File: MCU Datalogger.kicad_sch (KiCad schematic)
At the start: 0 parts

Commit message: Have added required symbols to schematic sheets.
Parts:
- added BT1: Battery, symbol Device:Battery
- added C1, C2, C3, C4, C5: C, symbol Device:C
- added C6: C_Polarized_US, symbol Device:C_Polarized_US
- added D1, D2: LED, symbol Device:LED
- added H1, H2, H3, H4: MountingHole, symbol Mechanical:MountingHole
- added R1, R2, R3, R4, R5, R6, R7: R_US, symbol Device:R_US
- added U1, U2: 24LC1025, symbol Memory_EEPROM:24LC1025
- added U3: DS1337S_, DS1337S_:SOIC127P600X175-8N, symbol DS1337S_:DS1337S_
- added U4: ATMEGA328P-AU, ATMEGA328P-AU:QFP80P900X900X120-32N, symbol ATMEGA328P-AU:ATMEGA328P-AU
- added Y1, Y2: Crystal, symbol Device:Crystal
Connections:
- new net: U4.21 (GND), U4.3 (GND), U4.5 (GND)
- new net: U4.4 (VCC), U4.6 (VCC)
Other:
- added sheet Connectors (connectors.kicad_sch)

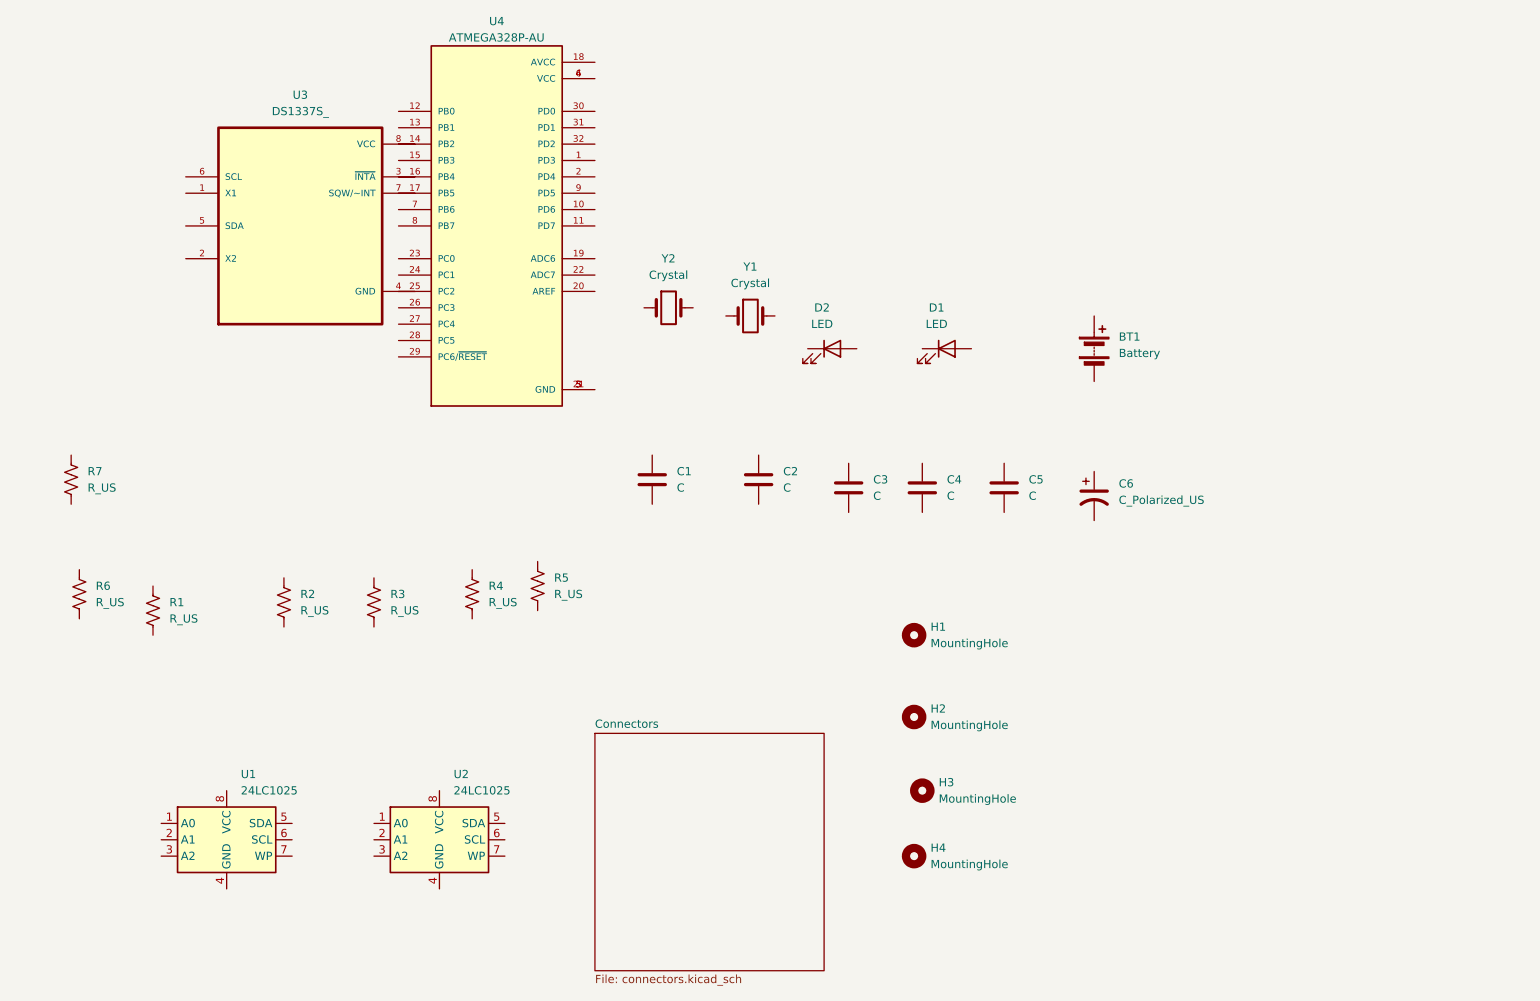
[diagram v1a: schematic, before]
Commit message: Changed locations of symbols (arrange).
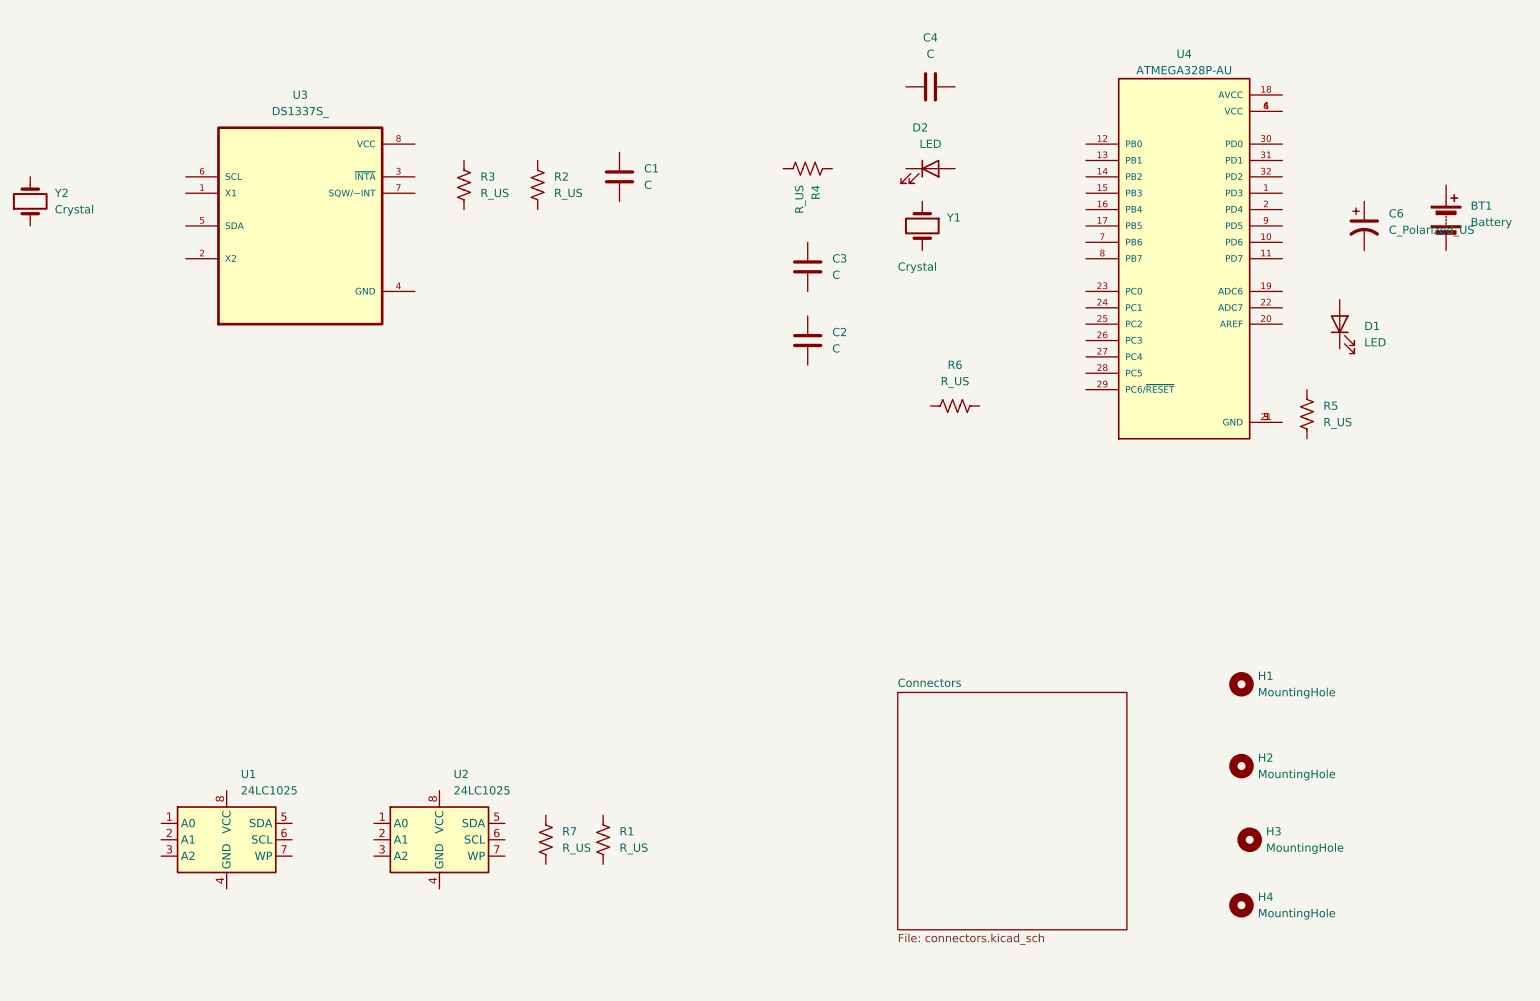
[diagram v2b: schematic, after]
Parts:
- removed C5: C, symbol Device:C
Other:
- moved on the sheet: BT1, C1, C2, C3, C4, C6, D1, D2, H1, H2, H3, H4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

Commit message: Added component values.
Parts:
- C1, C4: value C -> 0.1uF
- C2, C3: value C -> 22pF
- C6: value C_Polarized_US -> 100nF
- R1, R7: value R_US -> 4.7k
- R2, R3, R6: value R_US -> 10k
- R4, R5: value R_US -> 330
- Y1: value Crystal -> 16 MHz
- Y2: value Crystal -> 32.768 KHz
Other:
- moved on the sheet: C6
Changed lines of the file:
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@@
 			)
 		)
-		(property "Value" "C"
+		(property "Value" "22pF"
 			(at 166.37 63.4999 0)
 			(effects
@@
 			)
 		)
-		(property "Value" "Crystal"
+		(property "Value" "16 MHz"
 			(at 176.53 50.8 90)
 			(effects
@@
 			)
 		)
-		(property "Value" "R_US"
+		(property "Value" "4.7k"
 			(at 124.46 140.9699 0)
 			(effects
@@
 		(dnp no)
 		(property "Reference" "R4"
-			(at 163.8301 38.1 0)
-			(effects
-				(font
-					(size 1.27 1.27)
-				)
-				(justify left)
-			)
-		)
-		(property "Value" "R_US"
-			(at 161.2901 38.1 0)
+			(at 161.29 39.37 90)
+			(effects
+				(font
+					(size 1.27 1.27)
+				)
+				(justify left)
+			)
+		)
+		(property "Value" "330"
+			(at 160.02 31.75 90)
 			(effects
 				(font
@@
 			)
 		)
-		(property "Value" "R_US"
+		(property "Value" "4.7k"
 			(at 133.35 140.97 0)
 			(effects
@@
 			)
 		)
-		(property "Value" "C"
+		(property "Value" "0.1uF"
 			(at 181.61 17.78 90)
 			(effects
@@
 				)
 				(hide yes)
+			)
+		)
+		(property "Purpose" ""
+			(at 181.61 22.86 0)
+			(effects
+				(font
+					(size 1.27 1.27)
+				)
 			)
 		)
@@
 			)
 		)
-		(property "Value" "C"
+		(property "Value" "0.1uF"
 			(at 137.16 38.0999 0)
 			(effects
@@
 			)
 		)
-		(property "Value" "R_US"
+		(property "Value" "330"
 			(at 242.57 74.9299 0)
 			(effects
@@
 	(symbol
 		(lib_id "Device:C_Polarized_US")
-		(at 248.92 44.45 0)
+		(at 247.65 41.91 0)
 		(unit 1)
 		(exclude_from_sim no)
@@
 		(fields_autoplaced yes)
 		(property "Reference" "C6"
-			(at 252.73 42.5449 0)
-			(effects
-				(font
-					(size 1.27 1.27)
-				)
-				(justify left)
-			)
-		)
-		(property "Value" "C_Polarized_US"
-			(at 252.73 45.0849 0)
-			(effects
-				(font
-					(size 1.27 1.27)
-				)
-				(justify left)
-			)
-		)
-		(property "Footprint" ""
-			(at 248.92 44.45 0)
+			(at 251.46 40.0049 0)
+			(effects
+				(font
+					(size 1.27 1.27)
+				)
+				(justify left)
+			)
+		)
+		(property "Value" "100nF"
+			(at 251.46 42.5449 0)
+			(effects
+				(font
+					(size 1.27 1.27)
+				)
+				(justify left)
+			)
+		)
+		(property "Footprint" ""
+			(at 247.65 41.91 0)
 			(effects
 				(font
@@
 		)
 		(property "Datasheet" "~"
-			(at 248.92 44.45 0)
+			(at 247.65 41.91 0)
 			(effects
 				(font
@@
 		)
 		(property "Description" "Polarized capacitor, US symbol"
-			(at 248.92 44.45 0)
+			(at 247.65 41.91 0)
 			(effects
 				(font
@@
 			)
 		)
-		(property "Value" "R_US"
+		(property "Value" "10k"
 			(at 185.42 68.58 90)
 			(effects
@@
 			)
 		)
-		(property "Value" "R_US"
+		(property "Value" "10k"
 			(at 111.76 39.3699 0)
 			(effects
@@
 				)
 				(hide yes)
+			)
+		)
+		(property "Purpose" ""
+			(at 109.22 38.1 0)
+			(effects
+				(font
+					(size 1.27 1.27)
+				)
 			)
 		)
@@
 			)
 		)
-		(property "Value" "R_US"
+		(property "Value" "10k"
 			(at 123.19 39.3699 0)
 			(effects
@@
 			)
 		)
-		(property "Value" "Crystal"
+		(property "Value" "32.768 KHz"
 			(at 45.72 41.9099 90)
 			(effects
@@
 				)
 				(hide yes)
+			)
+		)
+		(property "Purpose" ""
+			(at 41.91 40.64 0)
+			(effects
+				(font
+					(size 1.27 1.27)
+				)
 			)
 		)
@@
 			)
 		)
-		(property "Value" "C"
+		(property "Value" "22pF"
 			(at 166.37 52.0699 0)
 			(effects

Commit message: Completed symbol-footprint associations.
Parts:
- BT1: footprint (none) -> Connector_PinHeader_2.54mm:PinHeader_1x02_P2.54mm_Vertical
- C1, C2, C3, C4, C6: footprint (none) -> Capacitor_SMD:C_0805_2012Metric
- D1, D2: footprint (none) -> LED_SMD:LED_0805_2012Metric
- H1, H2, H3, H4: footprint (none) -> MountingHole:MountingHole_2.1mm
- R1, R2, R3, R4, R5, R6, R7: footprint (none) -> Resistor_SMD:R_0805_2012Metric
- U1, U2: footprint (none) -> Package_SO:SOIC-8_5.23x5.23mm_P1.27mm
- U3: footprint DS1337S_:SOIC127P600X175-8N -> Footprints:SOIC127P600X175-8N
- U4: footprint ATMEGA328P-AU:QFP80P900X900X120-32N -> Footprints:QFP80P900X900X120-32N
- Y1, Y2: footprint (none) -> Crystal:Crystal_SMD_5032-2Pin_5.0x3.2mm_HandSoldering
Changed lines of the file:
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@@
 			)
 		)
-		(property "Footprint" ""
+		(property "Footprint" "Connector_PinHeader_2.54mm:PinHeader_1x02_P2.54mm_Vertical"
 			(at 261.62 41.656 90)
 			(effects
@@
 			)
 		)
-		(property "Footprint" ""
+		(property "Footprint" "MountingHole:MountingHole_2.1mm"
 			(at 231.14 139.7 0)
 			(effects
@@
 			)
 		)
-		(property "Footprint" ""
+		(property "Footprint" "MountingHole:MountingHole_2.1mm"
 			(at 229.87 128.27 0)
 			(effects
@@
 			)
 		)
-		(property "Footprint" ""
+		(property "Footprint" "Capacitor_SMD:C_0805_2012Metric"
 			(at 163.5252 66.04 0)
 			(effects
@@
 			)
 		)
-		(property "Footprint" ""
+		(property "Footprint" "Crystal:Crystal_SMD_5032-2Pin_5.0x3.2mm_HandSoldering"
 			(at 180.34 44.45 0)
 			(effects
@@
 			)
 		)
-		(property "Footprint" ""
+		(property "Footprint" "Resistor_SMD:R_0805_2012Metric"
 			(at 120.904 139.446 90)
 			(effects
@@
 			)
 		)
-		(property "Footprint" ""
+		(property "Footprint" "Resistor_SMD:R_0805_2012Metric"
 			(at 162.306 36.576 90)
 			(effects
@@
 			)
 		)
-		(property "Footprint" "ATMEGA328P-AU:QFP80P900X900X120-32N"
+		(property "Footprint" "Footprints:QFP80P900X900X120-32N"
 			(at 220.98 49.53 0)
 			(effects
@@
 			)
 		)
-		(property "Footprint" "DS1337S_:SOIC127P600X175-8N"
+		(property "Footprint" "Footprints:SOIC127P600X175-8N"
 			(at 83.82 44.45 0)
 			(effects
@@
 			)
 		)
-		(property "Footprint" ""
+		(property "Footprint" "Package_SO:SOIC-8_5.23x5.23mm_P1.27mm"
 			(at 105.41 139.7 0)
 			(effects
@@
 			)
 		)
-		(property "Footprint" ""
+		(property "Footprint" "Resistor_SMD:R_0805_2012Metric"
 			(at 131.826 139.954 90)
 			(effects
@@
 			)
 		)
-		(property "Footprint" ""
+		(property "Footprint" "Capacitor_SMD:C_0805_2012Metric"
 			(at 185.42 21.8948 0)
 			(effects
@@
 			)
 		)
-		(property "Footprint" ""
+		(property "Footprint" "Capacitor_SMD:C_0805_2012Metric"
 			(at 134.3152 40.64 0)
 			(effects
@@
 			)
 		)
-		(property "Footprint" ""
+		(property "Footprint" "Resistor_SMD:R_0805_2012Metric"
 			(at 241.046 73.914 90)
 			(effects
@@
 			)
 		)
-		(property "Footprint" ""
+		(property "Footprint" "Capacitor_SMD:C_0805_2012Metric"
 			(at 247.65 41.91 0)
 			(effects
@@
 			)
 		)
-		(property "Footprint" ""
+		(property "Footprint" "MountingHole:MountingHole_2.1mm"
 			(at 229.87 115.57 0)
 			(effects
@@
 			)
 		)
-		(property "Footprint" ""
+		(property "Footprint" "Resistor_SMD:R_0805_2012Metric"
 			(at 185.674 71.374 90)
 			(effects
@@
 			)
 		)
-		(property "Footprint" ""
+		(property "Footprint" "Resistor_SMD:R_0805_2012Metric"
 			(at 110.236 38.354 90)
 			(effects
@@
 			)
 		)
-		(property "Footprint" ""
+		(property "Footprint" "Resistor_SMD:R_0805_2012Metric"
 			(at 121.666 38.354 90)
 			(effects
@@
 			)
 		)
-		(property "Footprint" ""
+		(property "Footprint" "Package_SO:SOIC-8_5.23x5.23mm_P1.27mm"
 			(at 72.39 139.7 0)
 			(effects
@@
 			)
 		)
-		(property "Footprint" ""
+		(property "Footprint" "LED_SMD:LED_0805_2012Metric"
 			(at 181.61 35.56 0)
 			(effects
@@
 			)
 		)
-		(property "Footprint" ""
+		(property "Footprint" "LED_SMD:LED_0805_2012Metric"
 			(at 245.11 59.69 0)
 			(effects
@@
 			)
 		)
-		(property "Footprint" ""
+		(property "Footprint" "MountingHole:MountingHole_2.1mm"
 			(at 229.87 149.86 0)
 			(effects
@@
 			)
 		)
-		(property "Footprint" ""
+		(property "Footprint" "Crystal:Crystal_SMD_5032-2Pin_5.0x3.2mm_HandSoldering"
 			(at 41.91 40.64 0)
 			(effects
@@
 			)
 		)
-		(property "Footprint" ""
+		(property "Footprint" "Capacitor_SMD:C_0805_2012Metric"
 			(at 163.5252 54.61 0)
 			(effects
